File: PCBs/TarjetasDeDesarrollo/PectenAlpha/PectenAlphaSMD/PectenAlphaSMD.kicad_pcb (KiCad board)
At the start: 2 copper layers, 26 parts, among them J1 ICSP, J2 GPIO, Q1 PN2222A, SW1 SW_Push, SW2 SW_DIP_x04, U1 PIC_8-14-18-20, U2 D148K

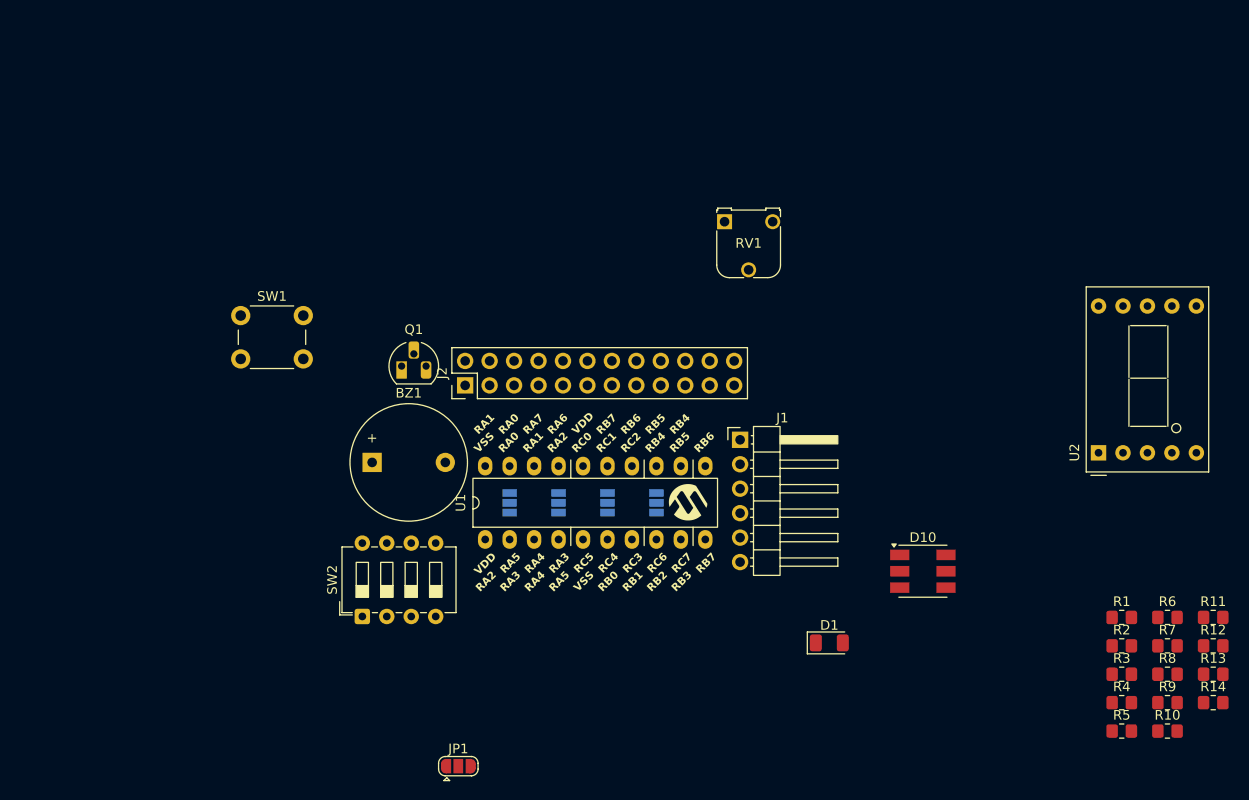
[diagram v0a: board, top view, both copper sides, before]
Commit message: Se tiene la PCB preliminar con forma de pecten alpha
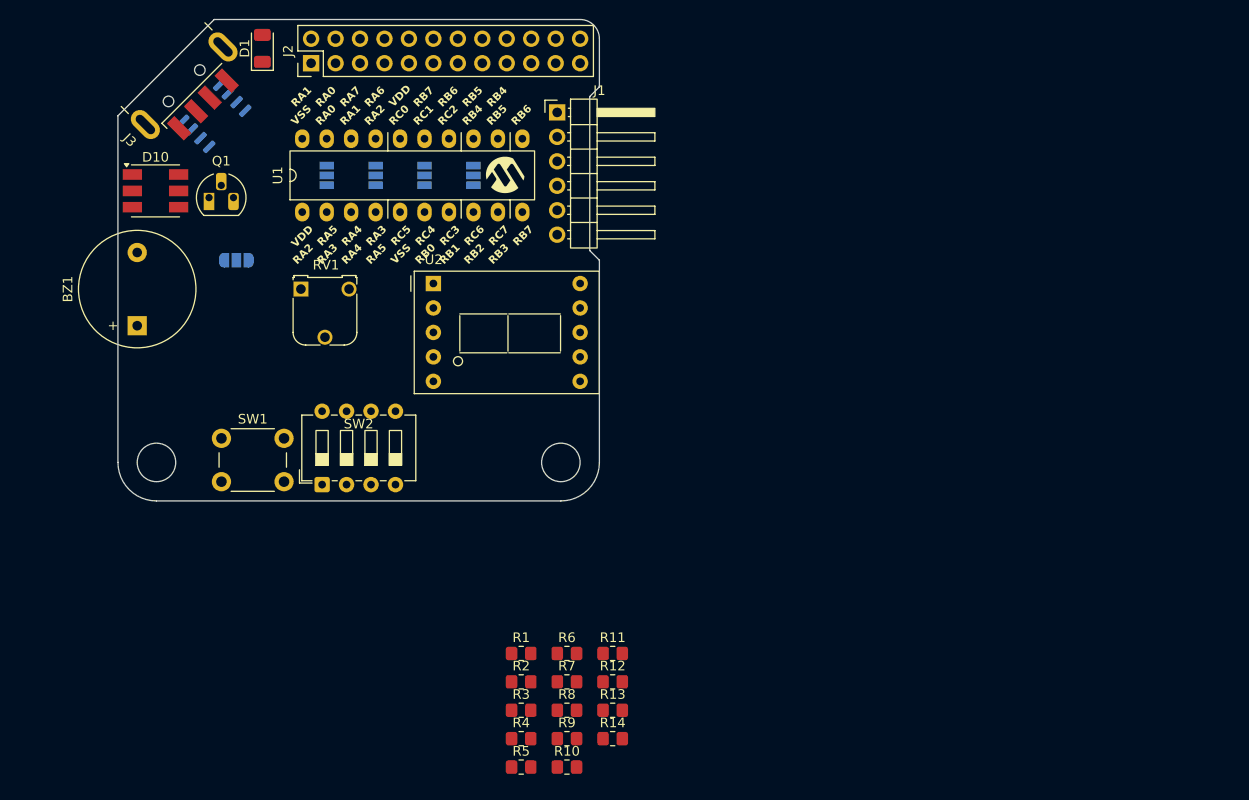
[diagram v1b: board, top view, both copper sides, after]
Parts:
- added J3: USB_A, Connector_USB:USB_A_CNCTech_1001-011-01101_Horizontal, F.Cu at (102.0, 32.0)
- added U3: CH340N, Package_SO:JEITA_SOIC-8_3.9x4.9mm_P1.27mm, B.Cu at (110.0, 40.0)
- JP1: moved to B.Cu
- moved D10 89.0 mm to (103.9, 47.8)
- moved D1 85.3 mm to (115.0, 33.0), turned to 90 degrees
- moved U2 71.3 mm to (132.8, 57.4), turned to 0 degrees
- moved R1 62.5 mm to (141.9, 95.8)
- moved R10 62.5 mm to (146.6, 107.6)
- moved R11 62.5 mm to (151.4, 95.8)
- moved R12 62.5 mm to (151.4, 98.8)
- moved R13 62.5 mm to (151.4, 101.7)
- moved R14 62.5 mm to (151.4, 104.7)
- moved R2 62.5 mm to (141.9, 98.8)
- moved R3 62.5 mm to (141.9, 101.7)
- moved R4 62.5 mm to (141.9, 104.7)
- moved R5 62.5 mm to (141.9, 107.6)
- moved R6 62.5 mm to (146.6, 95.8)
- moved R7 62.5 mm to (146.6, 98.8)
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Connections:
- R8 pad 1: /RC1/RB7 -> /RC2/RB6
- R9 pad 1: /RC2/RB6 -> /RC1/RB7
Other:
- board outline added: 50 x 50 mm

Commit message: Se inició una importante modificación de la tarjeta pectenAlpha
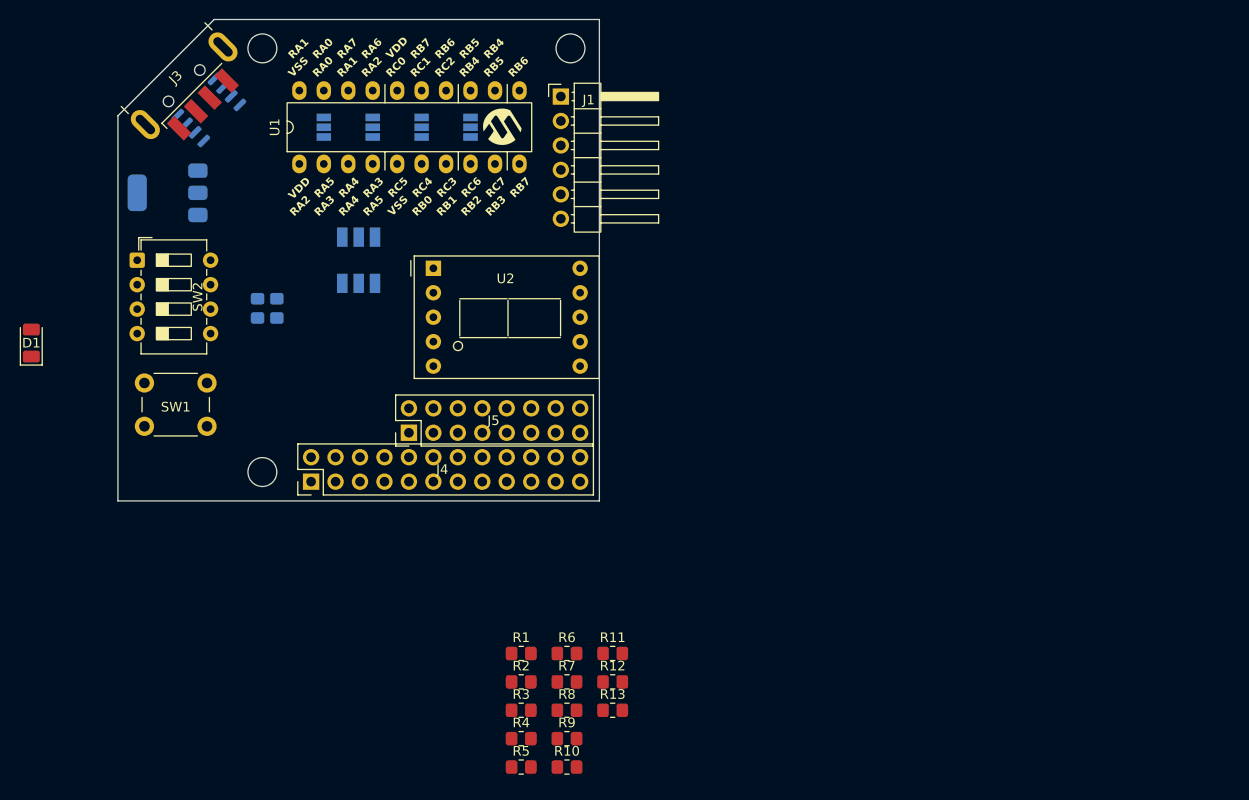
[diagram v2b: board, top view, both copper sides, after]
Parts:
- removed BZ1: Buzzer, Buzzer_Beeper:Buzzer_12x9.5RM7.6
- removed J2: GPIO, Connector_PinHeader_2.54mm:PinHeader_2x12_P2.54mm_Vertical
- removed JP1: PIN SEL, Jumper:SolderJumper-3_P1.3mm_Open_RoundedPad1.0x1.5mm
- removed Q1: PN2222A, Package_TO_SOT_THT:TO-92L_HandSolder
- removed R14: R_US, Resistor_SMD:R_0805_2012Metric_Pad1.20x1.40mm_HandSolder
- removed RV1: R_Pot_Trim_US, Potentiometer_THT:Potentiometer_Runtron_RM-065_Vertical
- added J4: PORT, Connector_PinHeader_2.54mm:PinHeader_2x12_P2.54mm_Vertical, F.Cu at (120.1, 78.0)
- added J5: EXPANSION, Connector_PinHeader_2.54mm:PinHeader_2x08_P2.54mm_Vertical, F.Cu at (130.2, 72.9)
- added R15: R_US, Resistor_SMD:R_0805_2012Metric_Pad1.20x1.40mm_HandSolder, B.Cu at (114.5, 60.0)
- added R16: R_US, Resistor_SMD:R_0805_2012Metric_Pad1.20x1.40mm_HandSolder, B.Cu at (116.5, 60.0)
- added U4: AMS1117-3.3, Package_TO_SOT_SMD:SOT-223-3_TabPin2, B.Cu at (105.2, 48.0)
- D1: value LED -> LED_ON
- D10: moved to B.Cu
- moved D1 38.9 mm to (91.0, 63.6)
- moved SW2 30.2 mm to (102.0, 55.0), turned to 0 degrees
- moved D10 22.3 mm to (125.0, 55.0), turned to -90 degrees
- moved SW1 9.85 mm to (102.8, 67.8)
- moved U1 5.01 mm to (129.0, 41.2)
- moved J1 1.69 mm to (146.0, 38.0)
- moved U2 1.58 mm to (132.8, 55.8)
- moved U3 0.82 mm to (109.4, 39.4)
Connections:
- J1 pad 5: VCC -> +5V
- J3 pad 1: Net-(J3-VBUS) -> +5V
- J3 pad 4: Net-(J3-GND) -> GND
- J3 pad 5: Net-(J3-GND) -> GND
- R2 pad 1: /RC4/RB0 -> unconnected-(R2-Pad1)
- R3 pad 1: /RC3/RB1 -> unconnected-(R3-Pad1)
- R4 pad 1: /RC6/RB2 -> unconnected-(R4-Pad1)
- R5 pad 1: /RC7/RB3 -> unconnected-(R5-Pad1)
- R6 pad 1: /RB5/RB4 -> unconnected-(R6-Pad1)
- R7 pad 1: /RB4/RB5 -> unconnected-(R7-Pad1)
- R8 pad 1: /RC2/RB6 -> unconnected-(R8-Pad1)
- R9 pad 1: /RC1/RB7 -> unconnected-(R9-Pad1)
- SW2 pad 4: /TRIM -> unconnected-(SW2-Pad4)
- SW2 pad 5: Net-(JP1-C) -> unconnected-(SW2-Pad5)
- SW2 pad 6: /BUZZER -> unconnected-(SW2-Pad6)
- U1 pad 21: VCC -> +5V
- U3 pad 3: Net-(J3-GND) -> GND
- U3 pad 5: Net-(J3-VBUS) -> +5V
- U3 pad 6: unconnected-(U3-TXD-Pad6) -> Net-(U3-TXD)
- U3 pad 7: unconnected-(U3-RXD-Pad7) -> Net-(U3-RXD)
- U3 pad 8: unconnected-(U3-V3-Pad8) -> Net-(U3-V3)
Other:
- outline, holes or cut-outs redrawn
